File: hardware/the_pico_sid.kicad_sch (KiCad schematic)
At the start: 10 parts, among them U1 SID_6581, U2 Pico

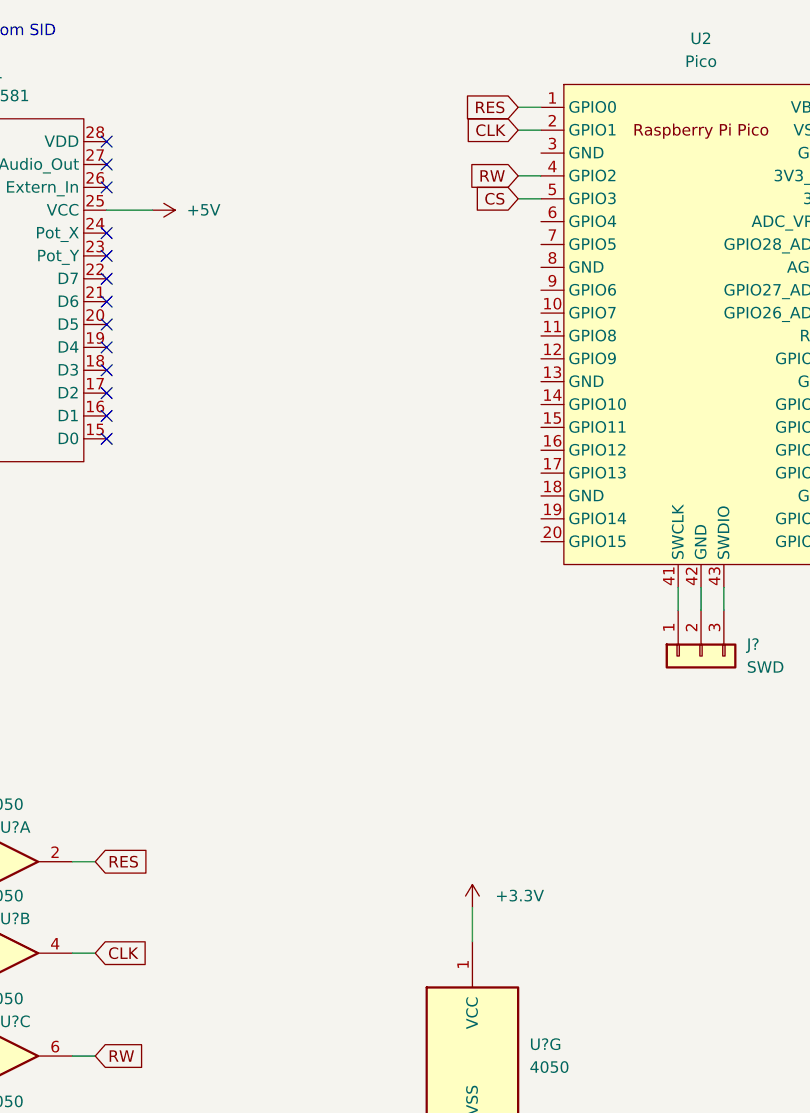
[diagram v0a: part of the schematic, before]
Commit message: added 100n, change pico pins for res, clk, cs, rw
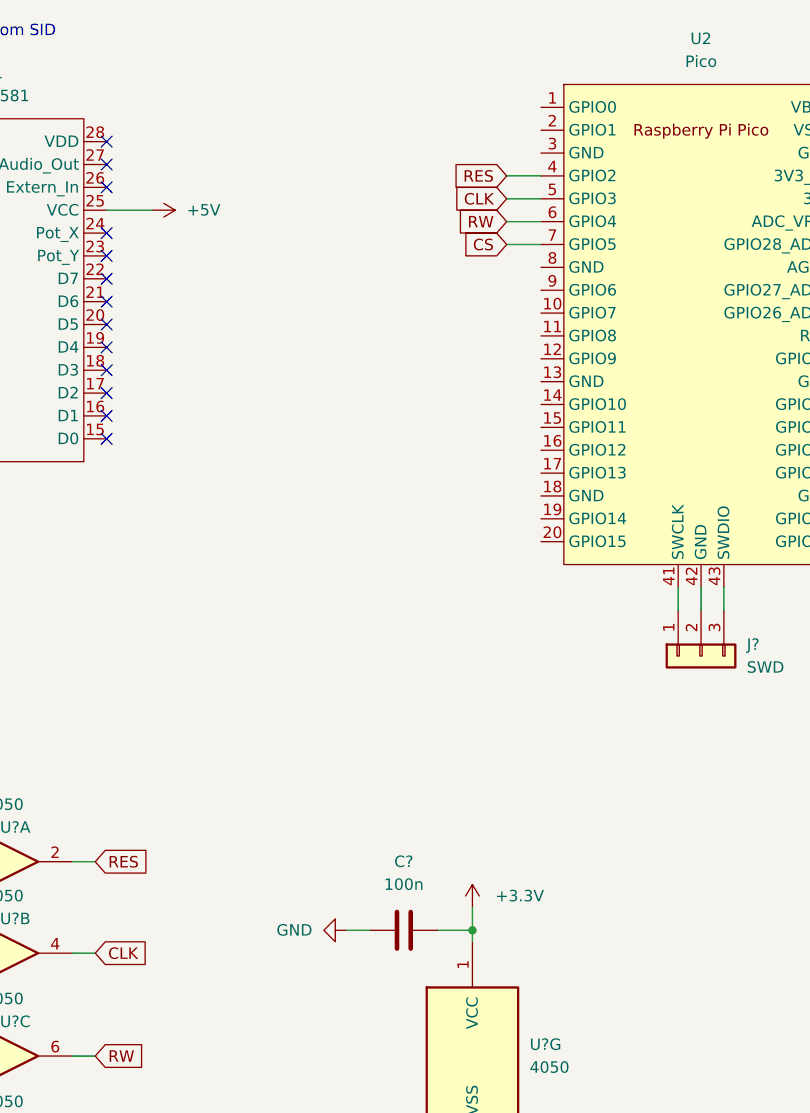
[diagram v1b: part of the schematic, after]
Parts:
- added C?: 100n, symbol Device:C
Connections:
- net +3.3V: now also C?.2
- net CLK: now also U2.5 (GPIO3); no longer U2.2 (GPIO1)
- net CS: now also U2.7 (GPIO5); no longer U2.5 (GPIO3)
- net GND: now also C?.1
- net RES: now also U2.4 (GPIO2); no longer U2.1 (GPIO0)
- net RW: now also U2.6 (GPIO4); no longer U2.4 (GPIO2)
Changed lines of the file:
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@@
     (company "Thorsten Kattanek")
+  )
+  (junction (at 100.33 116.84) (diameter 0) (color 0 0 0 0)
   )
   (no_connect (at 59.69 41.91))
@@
     (stroke (width 0) (type default) (color 0 0 0 0))
   )
+  (wire (pts (xy 104.14 40.64) (xy 107.95 40.64))
+    (stroke (width 0) (type default) (color 0 0 0 0))
+  )
   (wire (pts (xy 38.1 109.22) (xy 40.64 109.22))
     (stroke (width 0) (type default) (color 0 0 0 0))
   )
-  (wire (pts (xy 105.41 35.56) (xy 107.95 35.56))
+  (wire (pts (xy 100.33 116.84) (xy 100.33 118.11))
+    (stroke (width 0) (type default) (color 0 0 0 0))
+  )
+  (wire (pts (xy 104.14 38.1) (xy 107.95 38.1))
+    (stroke (width 0) (type default) (color 0 0 0 0))
+  )
+  (wire (pts (xy 104.14 33.02) (xy 107.95 33.02))
     (stroke (width 0) (type default) (color 0 0 0 0))
   )
@@
     (stroke (width 0) (type default) (color 0 0 0 0))
   )
-  (wire (pts (xy 105.41 33.02) (xy 107.95 33.02))
-    (stroke (width 0) (type default) (color 0 0 0 0))
-  )
   (wire (pts (xy 38.1 142.24) (xy 40.64 142.24))
     (stroke (width 0) (type default) (color 0 0 0 0))
@@
     (stroke (width 0) (type default) (color 0 0 0 0))
   )
-  (wire (pts (xy 105.41 27.94) (xy 107.95 27.94))
-    (stroke (width 0) (type default) (color 0 0 0 0))
-  )
   (wire (pts (xy 143.51 30.48) (xy 149.86 30.48))
     (stroke (width 0) (type default) (color 0 0 0 0))
@@
     (stroke (width 0) (type default) (color 0 0 0 0))
   )
+  (wire (pts (xy 86.36 116.84) (xy 88.9 116.84))
+    (stroke (width 0) (type default) (color 0 0 0 0))
+  )
   (wire (pts (xy 27.94 39.37) (xy 34.29 39.37))
     (stroke (width 0) (type default) (color 0 0 0 0))
@@
     (stroke (width 0) (type default) (color 0 0 0 0))
   )
-  (wire (pts (xy 105.41 25.4) (xy 107.95 25.4))
-    (stroke (width 0) (type default) (color 0 0 0 0))
-  )
-  (wire (pts (xy 100.33 114.3) (xy 100.33 118.11))
+  (wire (pts (xy 100.33 114.3) (xy 100.33 116.84))
+    (stroke (width 0) (type default) (color 0 0 0 0))
+  )
+  (wire (pts (xy 104.14 35.56) (xy 107.95 35.56))
+    (stroke (width 0) (type default) (color 0 0 0 0))
+  )
+  (wire (pts (xy 96.52 116.84) (xy 100.33 116.84))
     (stroke (width 0) (type default) (color 0 0 0 0))
   )
@@
     )
   )
-  (global_label "CS" (shape input) (at 105.41 35.56 180) (fields_autoplaced)
-    (effects (font (size 1.27 1.27)) (justify right))
-    (property "Referenzen zwischen Schaltplänen" "${INTERSHEET_REFS}" (id 0) (at 100.5174 35.6394 0)
+  (global_label "CS" (shape input) (at 104.14 40.64 180) (fields_autoplaced)
+    (effects (font (size 1.27 1.27)) (justify right))
+    (property "Referenzen zwischen Schaltplänen" "${INTERSHEET_REFS}" (id 0) (at 99.2474 40.7194 0)
       (effects (font (size 1.27 1.27)) (justify right) hide)
     )
@@
     )
   )
-  (global_label "RW" (shape input) (at 105.41 33.02 180) (fields_autoplaced)
-    (effects (font (size 1.27 1.27)) (justify right))
-    (property "Referenzen zwischen Schaltplänen" "${INTERSHEET_REFS}" (id 0) (at 100.2755 33.0994 0)
+  (global_label "RW" (shape input) (at 104.14 38.1 180) (fields_autoplaced)
+    (effects (font (size 1.27 1.27)) (justify right))
+    (property "Referenzen zwischen Schaltplänen" "${INTERSHEET_REFS}" (id 0) (at 99.0055 38.1794 0)
       (effects (font (size 1.27 1.27)) (justify right) hide)
     )
@@
     )
   )
-  (global_label "CLK" (shape input) (at 105.41 27.94 180) (fields_autoplaced)
-    (effects (font (size 1.27 1.27)) (justify right))
-    (property "Referenzen zwischen Schaltplänen" "${INTERSHEET_REFS}" (id 0) (at 99.4288 28.0194 0)
-      (effects (font (size 1.27 1.27)) (justify right) hide)
-    )
-  )
-  (global_label "RES" (shape input) (at 105.41 25.4 180) (fields_autoplaced)
-    (effects (font (size 1.27 1.27)) (justify right))
-    (property "Referenzen zwischen Schaltplänen" "${INTERSHEET_REFS}" (id 0) (at 99.3683 25.4794 0)
+  (global_label "CLK" (shape input) (at 104.14 35.56 180) (fields_autoplaced)
+    (effects (font (size 1.27 1.27)) (justify right))
+    (property "Referenzen zwischen Schaltplänen" "${INTERSHEET_REFS}" (id 0) (at 98.1588 35.6394 0)
+      (effects (font (size 1.27 1.27)) (justify right) hide)
+    )
+  )
+  (global_label "RES" (shape input) (at 104.14 33.02 180) (fields_autoplaced)
+    (effects (font (size 1.27 1.27)) (justify right))
+    (property "Referenzen zwischen Schaltplänen" "${INTERSHEET_REFS}" (id 0) (at 98.0983 33.0994 0)
       (effects (font (size 1.27 1.27)) (justify right) hide)
     )
@@
     (pin "8")
   )
+  (symbol (lib_id "Device:C") (at 92.71 116.84 90) (unit 1)
+    (in_bom yes) (on_board yes) (fields_autoplaced)
+    (property "Reference" "C?" (id 0) (at 92.71 109.22 90))
+    (property "Value" "100n" (id 1) (at 92.71 111.76 90))
+    (property "Footprint" "" (id 2) (at 96.52 115.8748 0)
+      (effects (font (size 1.27 1.27)) hide)
+    )
+    (property "Datasheet" "~" (id 3) (at 92.71 116.84 0)
+      (effects (font (size 1.27 1.27)) hide)
+    )
+    (pin "1")
+    (pin "2")
+  )
   (symbol (lib_id "4xxx:4050") (at 48.26 142.24 0) (unit 4)
     (in_bom yes) (on_board yes)
@@
     (pin "2")
     (pin "3")
+  )
+  (symbol (lib_id "power:GND") (at 86.36 116.84 270) (unit 1)
+    (in_bom yes) (on_board yes) (fields_autoplaced)
+    (property "Reference" "#PWR?" (id 0) (at 80.01 116.84 0)
+      (effects (font (size 1.27 1.27)) hide)
+    )
+    (property "Value" "GND" (id 1) (at 82.55 116.8399 90)
+      (effects (font (size 1.27 1.27)) (justify right))
+    )
+    (property "Footprint" "" (id 2) (at 86.36 116.84 0)
+      (effects (font (size 1.27 1.27)) hide)
+    )
+    (property "Datasheet" "" (id 3) (at 86.36 116.84 0)
+      (effects (font (size 1.27 1.27)) hide)
+    )
+    (pin "1")
   )
   (symbol (lib_id "4xxx:4050") (at 48.26 153.67 0) (unit 5)
@@
       (reference "#PWR?") (unit 1) (value "+3.3V") (footprint "")
     )
+    (path "/8011d12d-b89a-4bea-84dc-b58f556c0613"
+      (reference "#PWR?") (unit 1) (value "GND") (footprint "")
+    )
     (path "/c50baa0b-b7e5-42ae-8a9d-beadd2214ed0"
       (reference "#PWR?") (unit 1) (value "GND") (footprint "")
     )
+    (path "/249fc3f4-6214-43d5-bed7-4570a982ba76"
+      (reference "C?") (unit 1) (value "100n") (footprint "")
+    )
     (path "/6d20c440-e8ae-442d-9b38-e1d32399f02f"

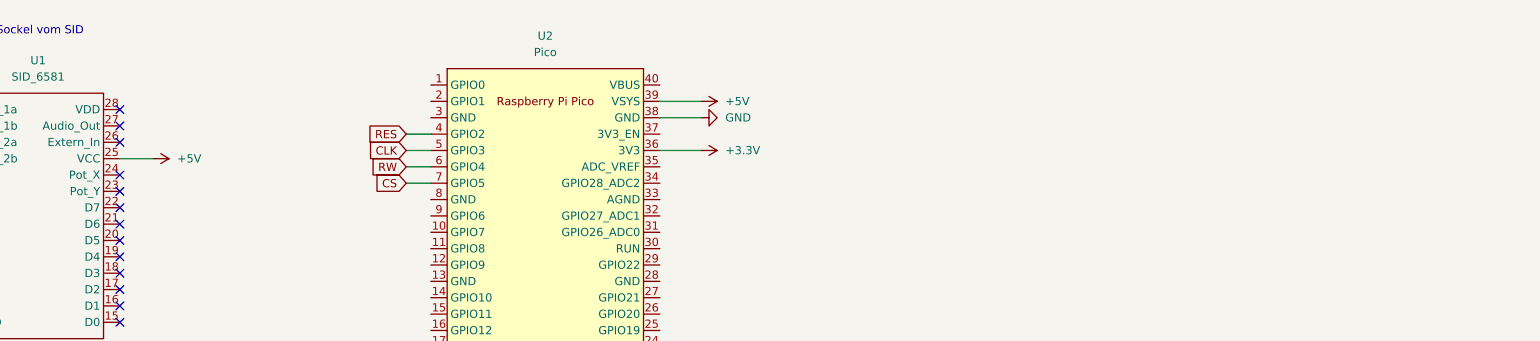
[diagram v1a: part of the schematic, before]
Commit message: added audio filter in schematic
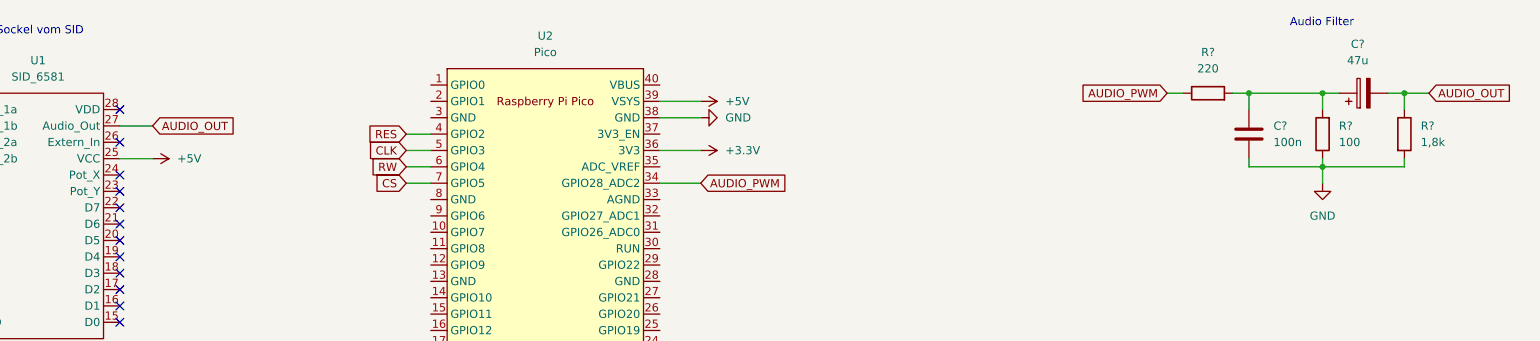
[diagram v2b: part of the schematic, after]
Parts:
- added C?: 100n, symbol Device:C
- added C?: 47u, symbol Device:C_Polarized
- added R?: 1,8k, symbol Device:R
- added R?: 220, symbol Device:R
- added R?: 100, symbol Device:R
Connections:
- net GND: now also C?.2, R?.1, R?.2
- net AUDIO_PWM: now reaches U2.34 (GPIO28_ADC2)
- net AUDIO_PWM: now also R?.1
- net AUDIO_OUT: now reaches U1.27 (Audio_Out)
- net AUDIO_OUT: now also C?.2, R?.1
- new net: C?.1, C?.1, R?.2, R?.2
- no-connect marks 22 -> 21
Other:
- note added: "Audio Filter"

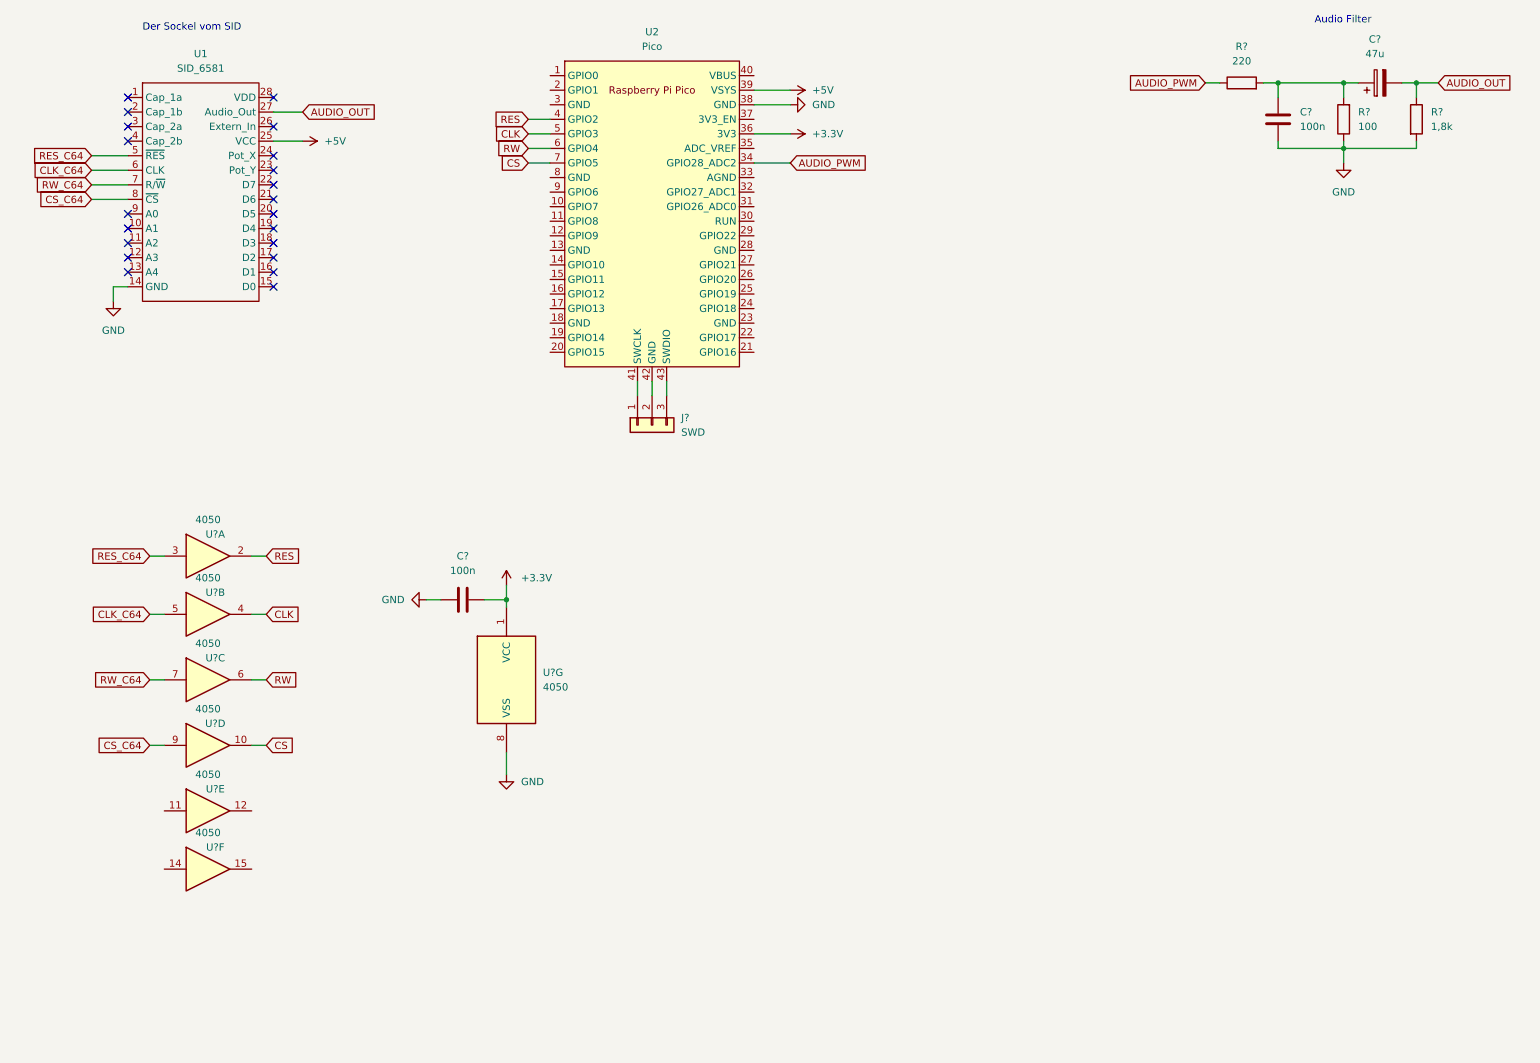
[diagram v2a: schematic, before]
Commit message: schematic: added five address lines from c64 to pico
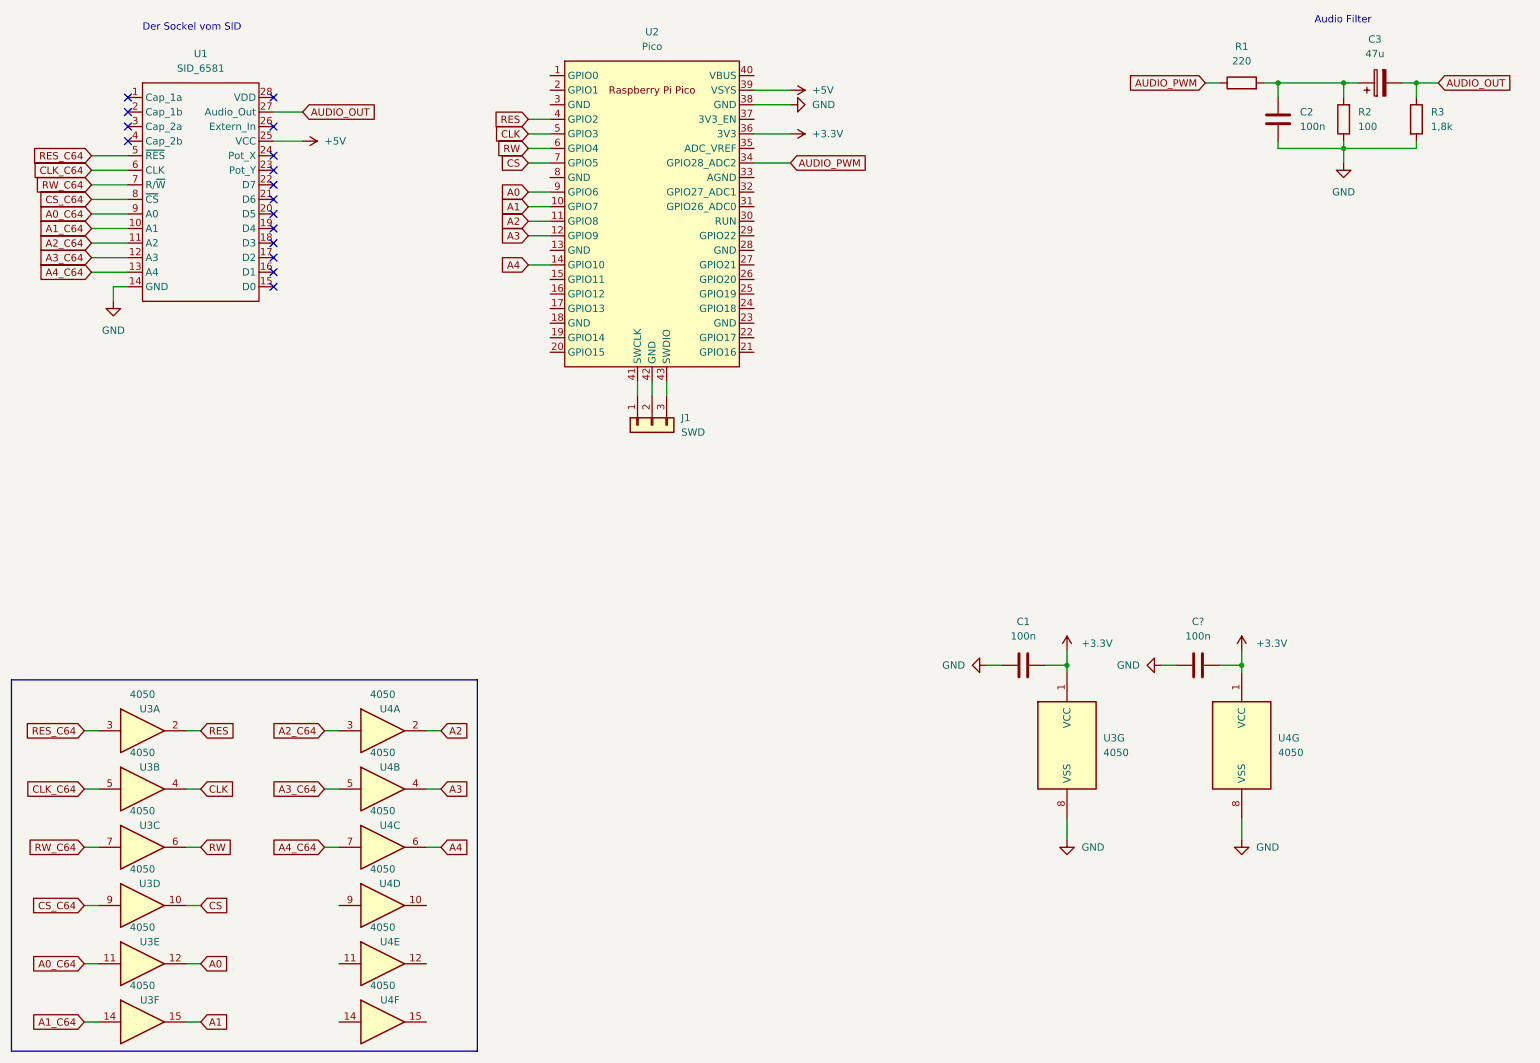
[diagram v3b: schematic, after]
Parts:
- added C?: 100n, symbol Device:C
- added U4: 4050, symbol 4xxx:4050
- gave numbers to parts that had none: 8
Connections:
- net +3.3V: now also C?.2, U4.1 (VCC)
- net GND: now also C?.1, U4.8 (VSS)
- net A0_C64: now reaches U3.11
- net A0_C64: now also U1.9 (A0)
- net A0: now reaches U3.12
- net A0: now also U2.9 (GPIO6)
- net A1_C64: now reaches U3.14
- net A1_C64: now also U1.10 (A1)
- net A1: now reaches U3.15
- net A1: now also U2.10 (GPIO7)
- net A2: now reaches U2.11 (GPIO8)
- net A2: now also U4.2
- net A3: now reaches U2.12 (GPIO9)
- net A3: now also U4.4
- net A4: now reaches U2.14 (GPIO10)
- net A4: now also U4.6
- net A2_C64: now reaches U1.11 (A2)
- net A2_C64: now also U4.3
- net A3_C64: now reaches U1.12 (A3)
- net A3_C64: now also U4.5
- net A4_C64: now reaches U1.13 (A4)
- net A4_C64: now also U4.7
- no-connect marks 21 -> 16
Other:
- moved on the sheet: C1, U3A, U3B, U3C, U3D, U3E, U3F, U3G
